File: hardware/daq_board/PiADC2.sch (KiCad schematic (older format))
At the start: 68 parts, among them J1 Pi GPIO, J2 ADCIN1, J3 ADCIN2, J4 ISO_IN_1, J5 ISO_IN_2, J6 I2C_OUT, SW1 SW_Push, SW2 SW_Push, U1 ADS1115IDGS, U2 TCA9517, U3 ADS1115IDGS, U4 24LC16, U5 MCP79401-I_SN, U6 MCP23008T-E_SS, U7 HCPL2631M, U8 HCPL2631M, Y1 Crystal

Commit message: Created breakout board and changed connectors
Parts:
- removed J4: ISO_IN_1, JST-XA:B04B-XASK-1(LF)(SN), symbol Connector:Conn_01x04_Male
- removed J5: ISO_IN_2, JST-XA:B04B-XASK-1(LF)(SN), symbol Connector:Conn_01x04_Male
- added J4: ISO_IN, OSTVN254:8POS, symbol Connector:Conn_01x08_Male
- J2, J3: footprint Connector_JST:JST_PUD_B10B-PUDSS_2x05_P2.00mm_Vertical -> AMPHENOL_75869-332LF:AMPHENOL_75869-332LF; symbol Connector_Generic:Conn_02x05_Odd_Even -> Connector_Generic:Conn_02x04_Odd_Even
- gave numbers to parts that had none: 2
- renumbered D5 to D2, D2 to D3, D6 to D4, D3 to D5, D7 to D6, D4 to D7
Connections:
- wire segments 310 -> 318
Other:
- moved on the sheet: R1, R10, R2, R3, R4, R7, R8, R9

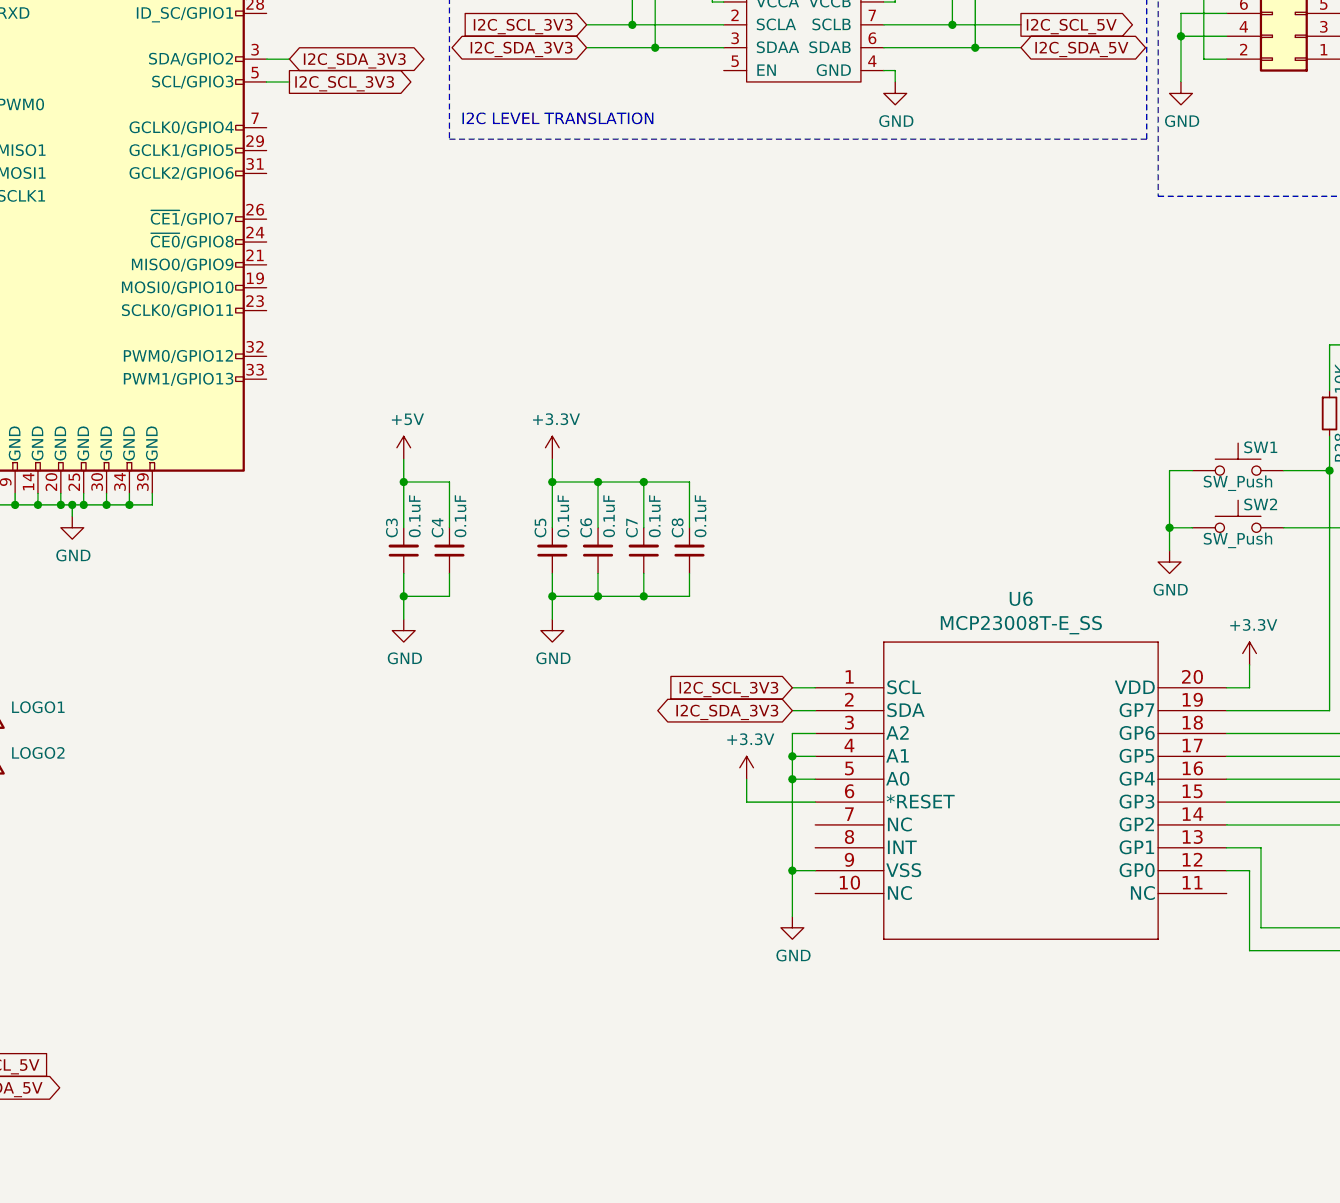
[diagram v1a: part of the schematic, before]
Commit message: Updated V2 to include an environmental sensor
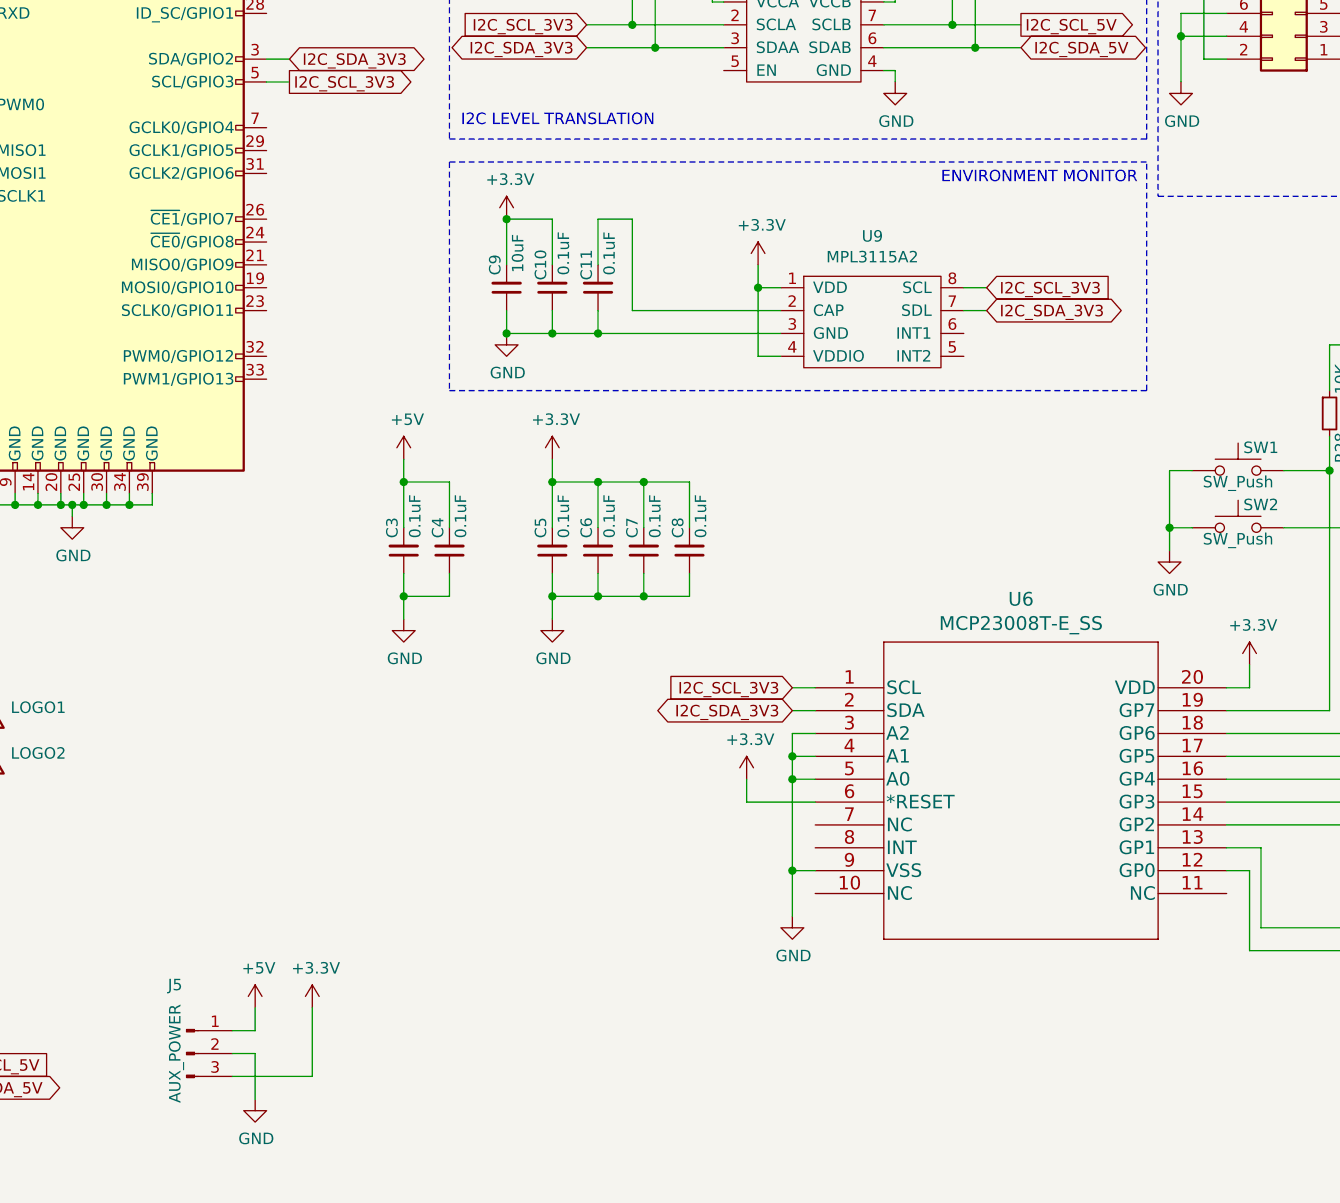
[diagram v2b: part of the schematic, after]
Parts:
- added C10, C11: 0.1uF, Capacitor_SMD:C_0603_1608Metric, symbol Device:C_Small
- added C9: 10uF, Capacitor_SMD:C_0603_1608Metric, symbol Device:C_Small
- added J5: AUX_POWER, Connector_PinHeader_2.54mm:PinHeader_1x03_P2.54mm_Vertical, symbol Connector:Conn_01x03_Male
- added U9: MPL3115A2, MPL3115A2:MPL3115A2, symbol MPL3115A2:MPL3115A2
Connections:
- net +3V3: now also C10.2, C9.2, J5.3 (Pin_3), U9.1 (VDD), U9.4 (VDDIO)
- net +5V: now also J5.1 (Pin_1)
- net GND: now also C10.1, C11.1, C9.1, J5.2 (Pin_2), U9.3 (GND)
- net I2C_SCL_3V3: now also U9.8 (SCL)
- net I2C_SDA_3V3: now also U9.7 (SDL)
- new net: C11.2, U9.2 (CAP)
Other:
- note added: "ENVIRONMENT MONITOR"
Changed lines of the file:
@@
 Wire Wire Line
 	9800 6450 10000 6450
+$Comp
+L MPL3115A2:MPL3115A2 U9
+U 1 1 5E3A58B4
+P 4900 4300
+F 0 "U9" H 4900 4675 50  0000 C CNN
+F 1 "MPL3115A2" H 4900 4584 50  0000 C CNN
+F 2 "MPL3115A2:MPL3115A2" H 4900 4100 50  0001 C CNN
+F 3 "" H 4900 4100 50  0001 C CNN
+	1    4900 4300
+	1    0    0    -1
+$EndComp
+$Comp
+L power:+3.3V #PWR0160
+U 1 1 5E3A6743
+P 3300 3850
+F 0 "#PWR0160" H 3300 3700 50  0001 C CNN
+F 1 "+3.3V" H 3315 4023 50  0000 C CNN
+F 2 "" H 3300 3850 50  0001 C CNN
+F 3 "" H 3300 3850 50  0001 C CNN
+	1    3300 3850
+	1    0    0    -1
+$EndComp
+$Comp
+L Device:C_Small C10
+U 1 1 5E3B54AB
+P 3500 4150
+F 0 "C10" V 3550 4050 50  0000 C CNN
+F 1 "0.1uF" V 3450 4000 50  0000 C CNN
+F 2 "Capacitor_SMD:C_0603_1608Metric" H 3500 4150 50  0001 C CNN
+F 3 "~" H 3500 4150 50  0001 C CNN
+	1    3500 4150
+	-1   0    0    1
+$EndComp
+$Comp
+L Device:C_Small C9
+U 1 1 5E3B60D3
+P 3300 4150
+F 0 "C9" V 3350 4050 50  0000 C CNN
+F 1 "10uF" V 3250 4000 50  0000 C CNN
+F 2 "Capacitor_SMD:C_0603_1608Metric" H 3300 4150 50  0001 C CNN
+F 3 "~" H 3300 4150 50  0001 C CNN
+	1    3300 4150
+	-1   0    0    1
+$EndComp
+$Comp
+L Device:C_Small C11
+U 1 1 5E3B652C
+P 3700 4150
+F 0 "C11" V 3750 4050 50  0000 C CNN
+F 1 "0.1uF" V 3650 4000 50  0000 C CNN
+F 2 "Capacitor_SMD:C_0603_1608Metric" H 3700 4150 50  0001 C CNN
+F 3 "~" H 3700 4150 50  0001 C CNN
+	1    3700 4150
+	-1   0    0    1
+$EndComp
+Wire Wire Line
+	3300 4250 3300 4350
+Wire Wire Line
+	3300 4350 3500 4350
+Wire Wire Line
+	3500 4250 3500 4350
+Connection ~ 3500 4350
+Wire Wire Line
+	3500 4350 3700 4350
+Wire Wire Line
+	3700 4250 3700 4350
+Connection ~ 3700 4350
+Wire Wire Line
+	3700 4350 4500 4350
+Wire Wire Line
+	3700 4050 3700 3850
+Wire Wire Line
+	3700 3850 3850 3850
+Wire Wire Line
+	3850 3850 3850 4250
+Wire Wire Line
+	3850 4250 4500 4250
+Wire Wire Line
+	3300 4050 3300 3850
+Wire Wire Line
+	3300 3850 3500 3850
+Wire Wire Line
+	3500 3850 3500 4050
+Connection ~ 3300 3850
+$Comp
+L power:+3.3V #PWR0161
+U 1 1 5E48AB2A
+P 4400 4050
+F 0 "#PWR0161" H 4400 3900 50  0001 C CNN
+F 1 "+3.3V" H 4415 4223 50  0000 C CNN
+F 2 "" H 4400 4050 50  0001 C CNN
+F 3 "" H 4400 4050 50  0001 C CNN
+	1    4400 4050
+	1    0    0    -1
+$EndComp
+Wire Wire Line
+	4400 4050 4400 4150
+Wire Wire Line
+	4400 4150 4500 4150
+Wire Wire Line
+	4500 4450 4400 4450
+Wire Wire Line
+	4400 4450 4400 4150
+Connection ~ 4400 4150
+$Comp
+L power:GND #PWR0162
+U 1 1 5E4C741A
+P 3300 4350
+F 0 "#PWR0162" H 3300 4100 50  0001 C CNN
+F 1 "GND" H 3305 4177 50  0000 C CNN
+F 2 "" H 3300 4350 50  0001 C CNN
+F 3 "" H 3300 4350 50  0001 C CNN
+	1    3300 4350
+	1    0    0    -1
+$EndComp
+Connection ~ 3300 4350
+Text GLabel 5400 4150 2    50   Input ~ 0
+I2C_SCL_3V3
+Text GLabel 5400 4250 2    50   BiDi ~ 0
+I2C_SDA_3V3
+Wire Wire Line
+	5400 4150 5300 4150
+Wire Wire Line
+	5300 4250 5400 4250
+Wire Notes Line
+	3050 3600 3050 4600
+Wire Notes Line
+	3050 4600 6100 4600
+Wire Notes Line
+	6100 4600 6100 3600
+Wire Notes Line
+	6100 3600 3050 3600
+Text Notes 5200 3700 0    50   ~ 0
+ENVIRONMENT MONITOR
+$Comp
+L Connector:Conn_01x03_Male J5
+U 1 1 5E576361
+P 1900 7500
+F 0 "J5" H 1850 7800 50  0000 C CNN
+F 1 "AUX_POWER" V 1850 7500 50  0000 C CNN
+F 2 "Connector_PinHeader_2.54mm:PinHeader_1x03_P2.54mm_Vertical" H 1900 7500 50  0001 C CNN
+F 3 "~" H 1900 7500 50  0001 C CNN
+	1    1900 7500
+	1    0    0    -1
+$EndComp
+$Comp
+L power:+5V #PWR0163
+U 1 1 5E5770BD
+P 2200 7300
+F 0 "#PWR0163" H 2200 7150 50  0001 C CNN
+F 1 "+5V" H 2215 7473 50  0000 C CNN
+F 2 "" H 2200 7300 50  0001 C CNN
+F 3 "" H 2200 7300 50  0001 C CNN
+	1    2200 7300
+	1    0    0    -1
+$EndComp
+$Comp
+L power:GND #PWR0164
+U 1 1 5E57791C
+P 2200 7700
+F 0 "#PWR0164" H 2200 7450 50  0001 C CNN
+F 1 "GND" H 2205 7527 50  0000 C CNN
+F 2 "" H 2200 7700 50  0001 C CNN
+F 3 "" H 2200 7700 50  0001 C CNN
+	1    2200 7700
+	1    0    0    -1
+$EndComp
+Wire Wire Line
+	2100 7400 2200 7400
+Wire Wire Line
+	2200 7400 2200 7300
+Wire Wire Line
+	2100 7500 2200 7500
+Wire Wire Line
+	2200 7500 2200 7700
+$Comp
+L power:+3.3V #PWR0165
+U 1 1 5E5B915E
+P 2450 7300
+F 0 "#PWR0165" H 2450 7150 50  0001 C CNN
+F 1 "+3.3V" H 2465 7473 50  0000 C CNN
+F 2 "" H 2450 7300 50  0001 C CNN
+F 3 "" H 2450 7300 50  0001 C CNN
+	1    2450 7300
+	1    0    0    -1
+$EndComp
+Wire Wire Line
+	2100 7600 2450 7600
+Wire Wire Line
+	2450 7600 2450 7300
 $EndSCHEMATC

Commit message: Updated rescue files to actually work with symbols in schematic now
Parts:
- U2: symbol tca9517:TCA9517 -> PiADC2-rescue:TCA9517-tca9517
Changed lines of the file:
@@
 	10050 1250 9850 1250
 $Comp
-L tca9517:TCA9517 U2
+L PiADC2-rescue:TCA9517-tca9517 U2
 U 1 1 5E193341
 P 4600 3100
